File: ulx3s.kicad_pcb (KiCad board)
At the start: 4 copper layers, 94 x 50.8 mm, 148 parts, among them J1 CONN_02X20, J2 CONN_02X20, J3 WIFI_OFF, J4 CONN_02X03, J5 VJ1, Q1 BC857, Q2 2N7002, U1 LFE5U-85F-6BG381C, U10 IS25LP128F-JBLE, U2 MT48LC16M16A2TG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

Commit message: rewire all the things
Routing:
- net GND: track 431.6 -> 440.7 mm, vias 146 -> 147
- net BTN_R: track 63.4 -> 71.7 mm
- net GP18: track 47.1 -> 54.4 mm
- net GN18: track 45.0 -> 50.3 mm
- net GP17: track 58.0 -> 62.3 mm
- net GN17: track 45.5 -> 49.0 mm
- net /flash/FPGA_PROGRAMN: track 38.4 -> 41.2 mm
- net SDRAM_D9: track 18.2 -> 20.8 mm
- net SDRAM_DQM1: track 22.4 -> 25.1 mm
- net SDRAM_D8: track 20.9 -> 23.3 mm
- net SDRAM_D10: track 18.3 -> 20.7 mm
- net BTN_F2: track 24.2 -> 21.9 mm
- net SDRAM_CLK: track 24.3 -> 26.5 mm
- net GN12: track 44.1 -> 46.1 mm
- net SDRAM_A12: track 26.1 -> 27.8 mm
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
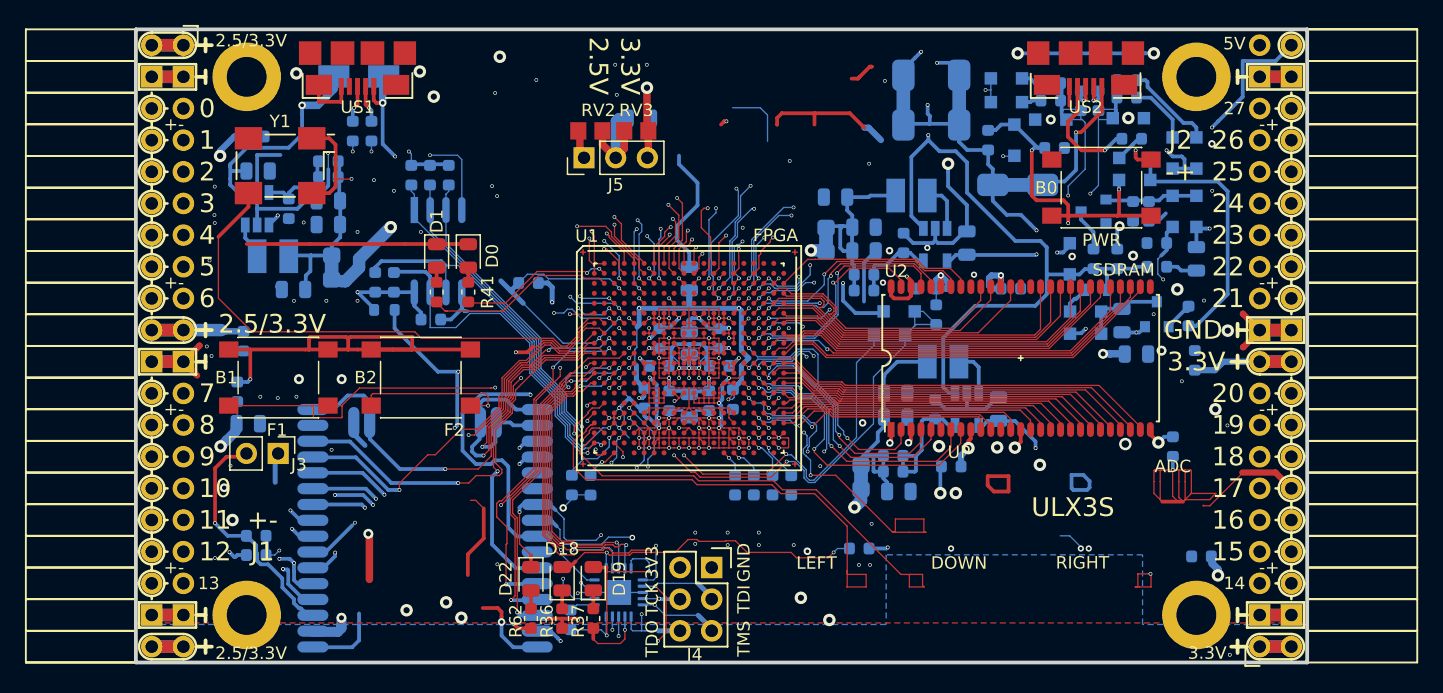
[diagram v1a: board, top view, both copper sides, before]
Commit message: remove btn_r, clean trace/via
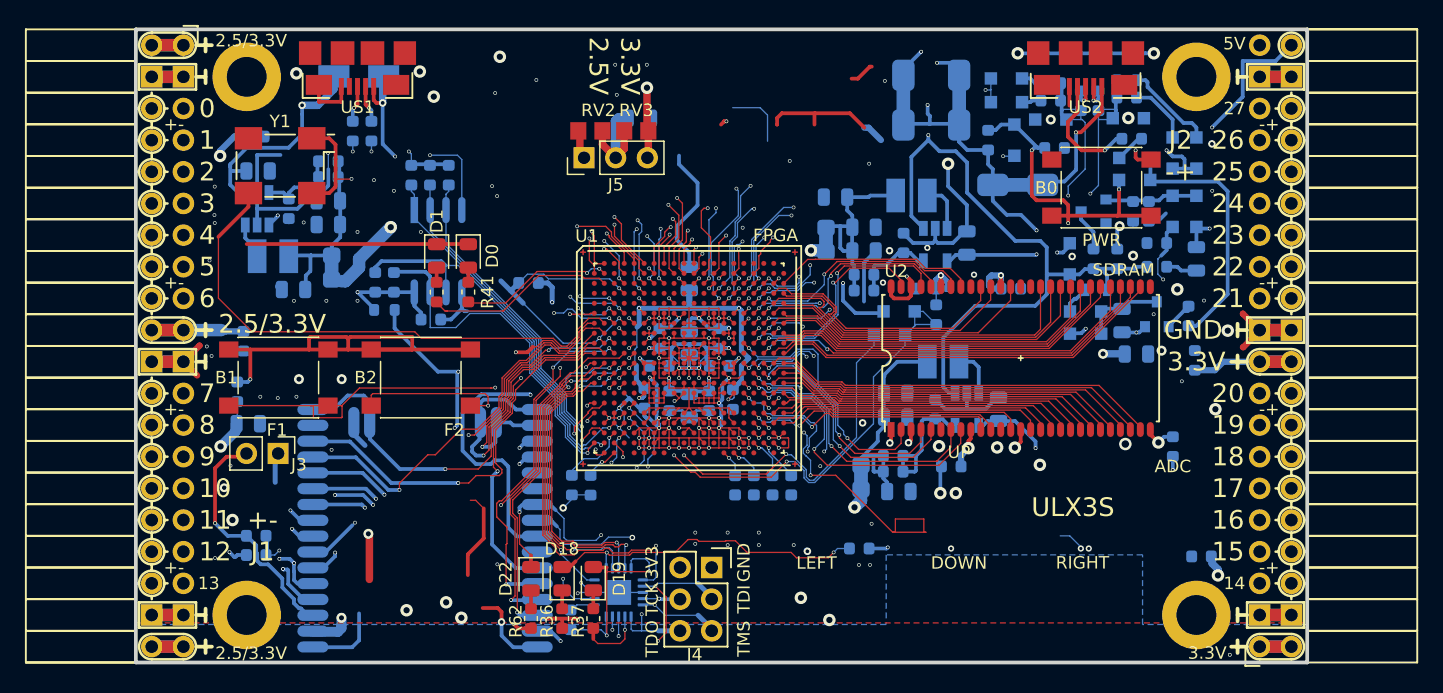
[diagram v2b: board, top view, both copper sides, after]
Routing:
- net BTN_R: track 71.7 -> 0.00 mm, vias 4 -> 0
- net BTN_L: track 37.6 -> 0.00 mm
- net BTN_D: track 36.9 -> 0.00 mm
- net GND: track 440.7 -> 414.8 mm
- net (no net): track 10.3 -> 0.00 mm
- net GP17: track 62.3 -> 53.5 mm
- net +3V3: track 162.3 -> 161.2 mm
- net SDRAM_D15: track 17.3 -> 16.6 mm
- net SDRAM_D13: track 17.5 -> 17.0 mm

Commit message: mark other button as no-connect, remove tracks
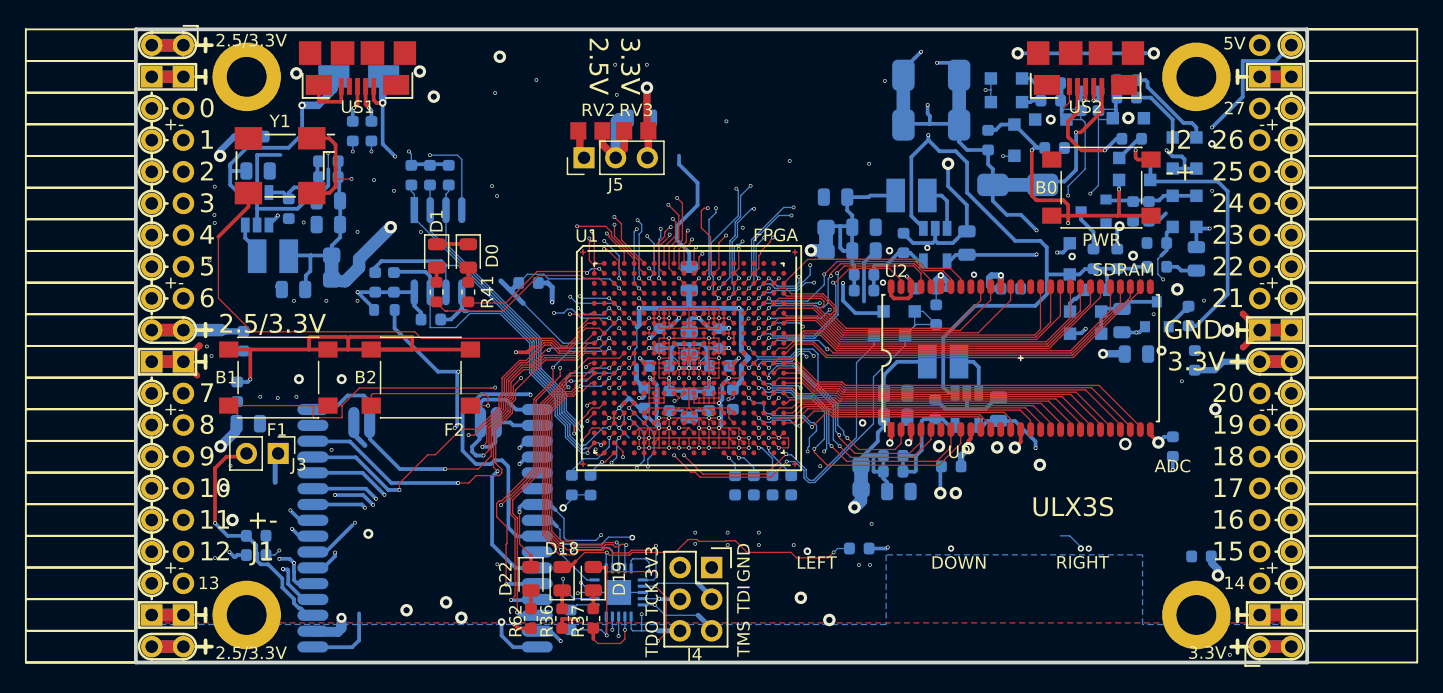
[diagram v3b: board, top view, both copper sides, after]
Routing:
- net GND: track 414.8 -> 365.1 mm
- net +3V3: track 161.2 -> 135.9 mm
- net BTN_U: track 24.0 -> 0.00 mm, vias 3 -> 0
